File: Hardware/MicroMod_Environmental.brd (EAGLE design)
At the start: 46.5 x 38 mm, 26 parts, among them J1 MICROMOD_STANDARD, U1 SGP40, U3 SHTC3, U4 3.3V, U5 STC31

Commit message: Routed
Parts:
- added U2: EEPROM, SparkFun-IC-Memory:SO08
- C3, C4: device SparkFun-Capacitors:0603@1 -> SparkFun-Capacitors:0603
- C5, C6: device SparkFun-Capacitors:0402-TIGHT -> SparkFun-Capacitors:0603
- R12: value 100K -> 100k; device SparkFun-Resistors:0402 -> SparkFun-Resistors:0603
- R3: device SparkFun-Resistors:0402-TIGHT -> SparkFun-Resistors:0603
- moved R1 90.1 mm to (11.0, 13.1), turned to 270 degrees
- moved R2 88.3 mm to (9.02, 13.1), turned to 270 degrees
- moved R12 68.8 mm to (8.89, 29.2), turned to 90 degrees
- moved U4 61.4 mm to (13.0, 29.2), turned to 270 degrees
- moved C6 60.1 mm to (12.7, 32.0)
- moved C5 53.5 mm to (16.6, 31.2), turned to 90 degrees
- moved R3 47.1 mm to (62.2, 2.67)
- moved PWR\ 46.6 mm to (62.2, 6.93), turned to 180 degrees
- moved LED2 45.8 mm to (62.1, 4.57)
- moved C4 38.5 mm to (29.3, 19.3), turned to 90 degrees
- moved JP1 38.4 mm to (9.91, 10.2)
- moved 0X2A 36.7 mm to (28.3, 29.0)
- moved R6 36.2 mm to (25.0, 33.9)
- moved R5 32.2 mm to (25.0, 31.5)
- moved U5 32.1 mm to (33.8, 19.1), turned to 270 degrees
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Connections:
- removed net GND1: LED2.C
- new net A0: J1.36, U2.1
- new net A1: J1.34, U2.2
- new net A2: J1.32, U2.3
- net 3.3V: now also U2.8; no longer J1.73
- net GND: now also LED2.C, U2.4, U2.7
- net SCL: now also U2.6
- net SDA: now also U2.5
- net VCC: now also J1.72, J1.74
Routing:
- net 3.3V: track 0.00 -> 132.5 mm, vias 0 -> 5
- net SCL: track 0.00 -> 102.3 mm, vias 0 -> 2
- net SDA: track 0.00 -> 96.0 mm, vias 0 -> 2
- net ADDR: track 0.00 -> 19.4 mm, vias 0 -> 2
- net VCC: track 0.00 -> 11.3 mm, vias 0 -> 1
- net EN: track 0.00 -> 10.9 mm
- net A0: track 0.00 -> 8.10 mm, vias 0 -> 1
- net A1: track 0.00 -> 7.78 mm, vias 0 -> 1
- net A2: track 0.00 -> 7.46 mm, vias 0 -> 1
- net N$2: track 0.00 -> 6.95 mm, vias 0 -> 2
- net N$1: track 0.00 -> 4.88 mm
- net GND: track 0.00 -> 3.43 mm, vias 0 -> 16
- net N$3: track 0.00 -> 2.26 mm
- net N$4: track 0.00 -> 2.13 mm
- net N$7: track 0.00 -> 2.07 mm
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- added copper zone on layer 1, net 3.3V
- added copper zone on layer 1, net GND
- added copper zone on layer 16, net GND
- added copper zone on layer 16, net VCC
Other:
- board size 46.5 x 38 mm -> 65 x 38 mm

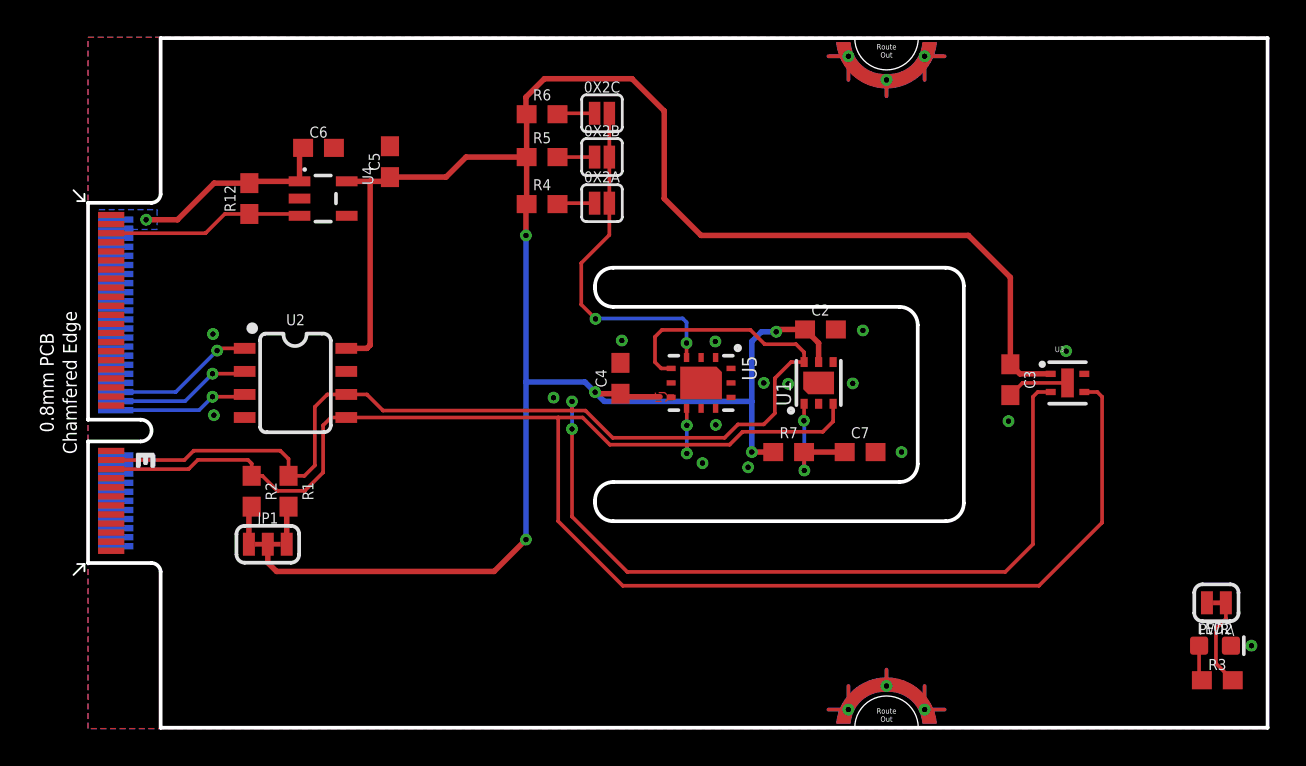
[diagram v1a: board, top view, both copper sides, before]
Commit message: Small tweaks to traces
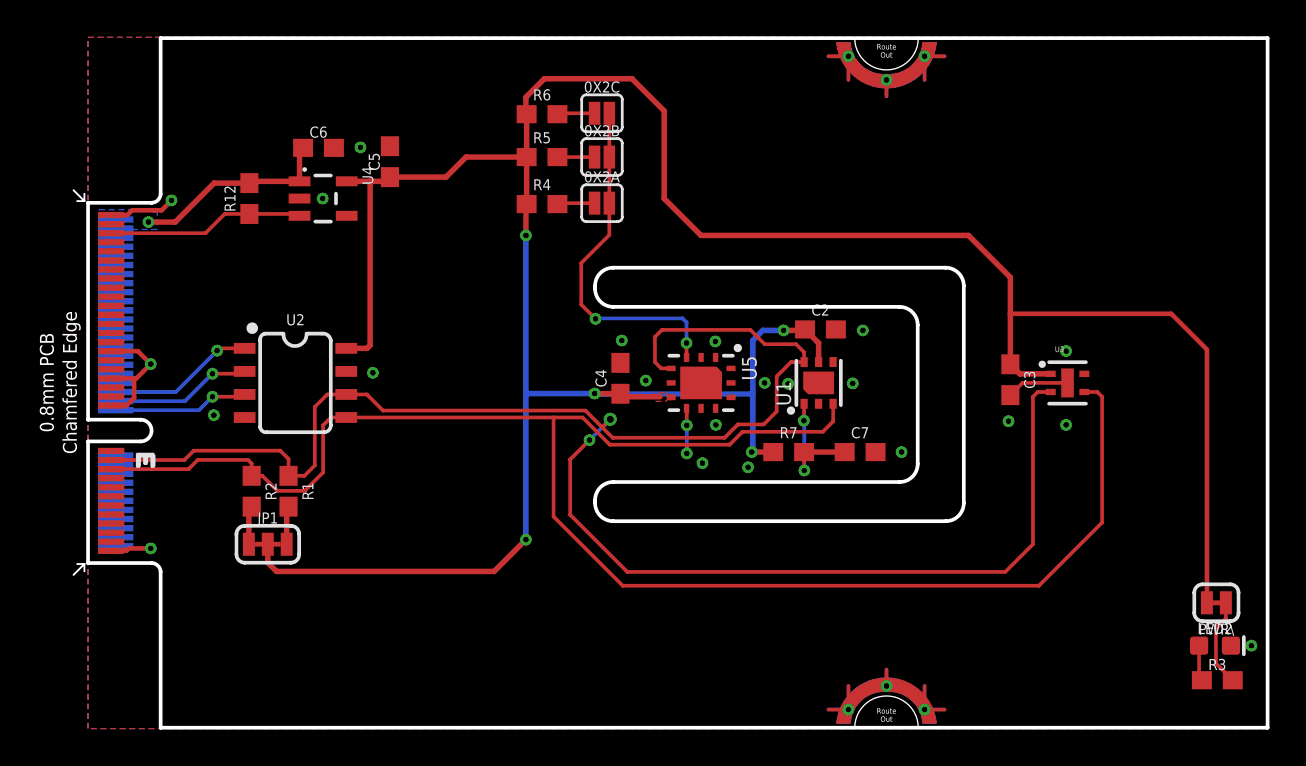
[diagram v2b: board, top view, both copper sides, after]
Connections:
- removed net 3.3V1: PWR\.2
- net 3.3V: now also PWR\.2
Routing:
- net 3.3V: track 132.5 -> 157.7 mm
- net GND: track 3.43 -> 27.4 mm, vias 16 -> 22

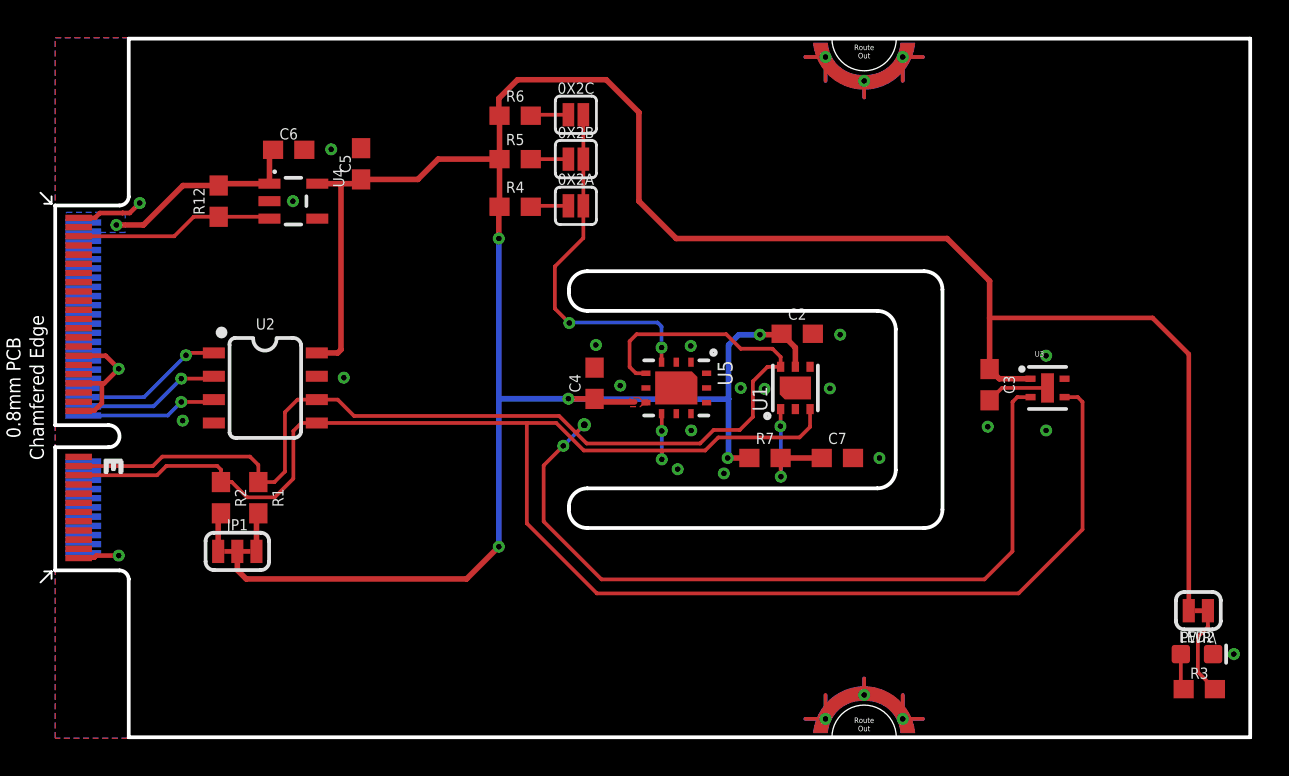
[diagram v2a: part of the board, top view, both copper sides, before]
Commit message: Adds silk, fiducials, and version number
* Adds text to part boxes in schematic
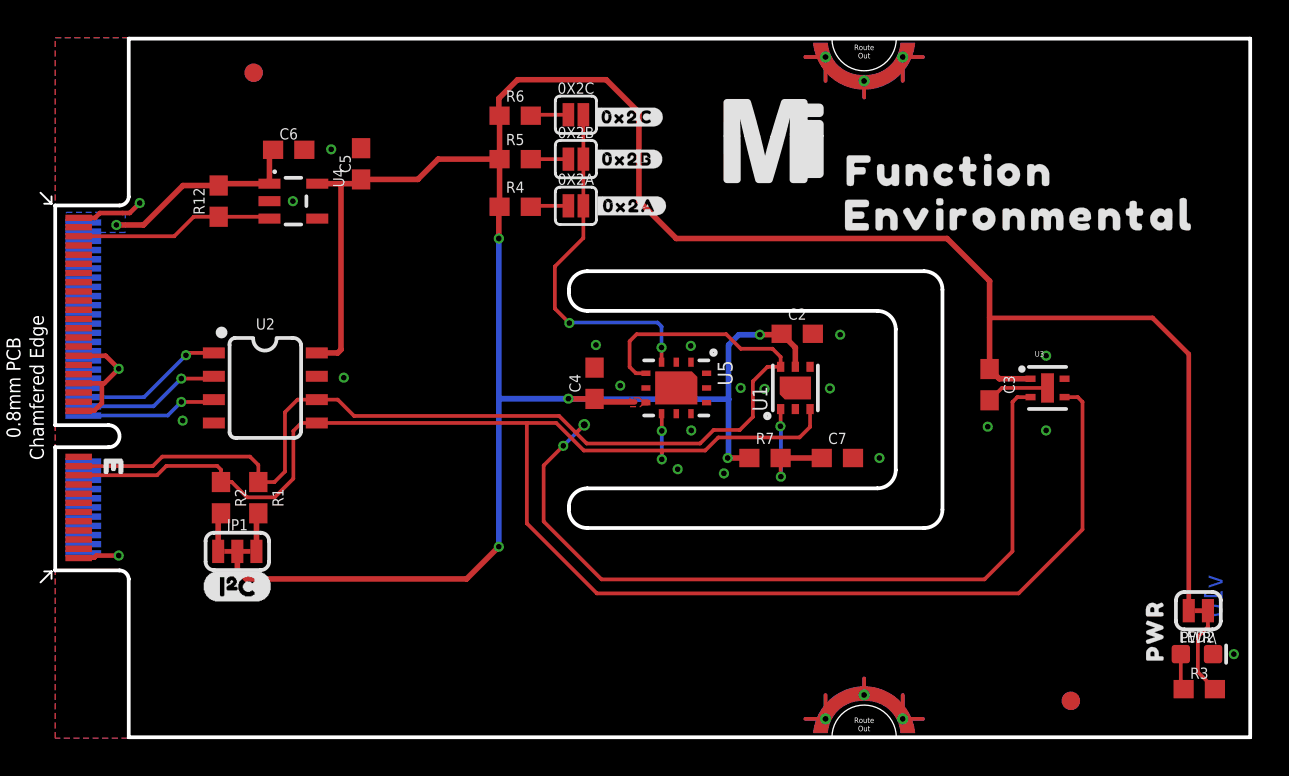
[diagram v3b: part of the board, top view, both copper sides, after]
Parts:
- added FD1, FD2, FD3, FD4: FIDUCIAL1X2, SparkFun-Aesthetics:FIDUCIAL-1X2
- added LOGO1: SFE_LOGO_NAME_FLAME.2_INCH, SparkFun-Aesthetics:SFE_LOGO_NAME_FLAME_.2
- added LOGO2: OSHW-LOGOS, SparkFun-Aesthetics:OSHW-LOGO-S
- added U$1: (no value), top:#0X2A#21
- added U$2: (no value), top:#0X2B#21
- added U$3: (no value), top:#0X2C#21
- added U$4: (no value), top:PWR321541
- added U$5: (no value), top:FUNCTION524
- added U$6: (no value), top:ENVIRONMENTAL526
- added U$7: (no value), SparkFun-MicroMod:MICROMOD_MI_LOGO_1
- added U$8: (no value), SparkFun-Buzzard:I2C
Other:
- board text added: "v10"
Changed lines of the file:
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@@
 <setting verticaltext="up"/>
 </settings>
-<grid distance="0.01" unitdist="inch" unit="inch" style="dots" multiple="1" display="yes" altdistance="0.001" altunitdist="inch" altunit="inch"/>
+<grid distance="0.05" unitdist="inch" unit="inch" style="dots" multiple="1" display="yes" altdistance="0.005" altunitdist="inch" altunit="inch"/>
 <layers>
 <layer number="1" name="Top" color="4" fill="1" visible="yes" active="yes"/>
@@
 <wire x1="28.94" y1="11.43" x2="47.26" y2="11.43" width="0.2032" layer="20"/>
 <wire x1="28.94" y1="13.589" x2="27.94" y2="12.589" width="0.2032" layer="20" curve="90"/>
+<text x="63.5" y="8.89" size="1.016" layer="16" font="vector" ratio="20" rot="SMR270">v10</text>
 </plain>
 <attributes>
@@
 </class>
 </classes>
-<designrules name="SparkFun-2-Layer-General-JLCPCB">
-<description language="en">&lt;b&gt;2 Layer General Rules for JLCPCB&lt;/b&gt;
+<designrules name="SparkFun-2-Layer-Minimum-JLCPCB">
+<description language="en">&lt;b&gt;2 Layer Minimum Rules for JLCPCB&lt;/b&gt;
 &lt;p&gt;
-These are the free and generally easy to produce 2-layer PCB design rules. You can certainly go smaller but if the design doesn't call for it, these rules provide good guidance.
+These are the minimums &lt;a href=&quot;https://jlcpcb.com/capabilities/Capabilities&quot;&gt;quoted by JLCPCB&lt;/a&gt; to produce a 2-layer PCB design rules. These rules are &quot;free&quot; and generally low-cost. Going below these settings may cause the board to be not manufacturable or incur a price increase.
 &lt;ul&gt;
 &lt;li&gt;2 Layer&lt;/li&gt;
-&lt;li&gt;7mil Trace/Space&lt;/li&gt;
-&lt;li&gt;7mil Annular Rings&lt;/li&gt;
+&lt;li&gt;5mil Trace/Space&lt;/li&gt;
+&lt;li&gt;5mil Annular Rings&lt;/li&gt;
 &lt;li&gt;12mil Vias&lt;/li&gt;
-&lt;li&gt;3mil Stop Mask&lt;/li&gt;
+&lt;li&gt;2.5mil Stop Mask&lt;/li&gt;
 &lt;/ul&gt;</description>
 <param name="layerSetup" value="(1*16)"/>
 <param name="mtCopper" value="0.035mm 0.035mm 0.035mm 0.035mm 0.035mm 0.035mm 0.035mm 0.035mm 0.035mm 0.035mm 0.035mm 0.035mm 0.035mm 0.035mm 0.035mm 0.035mm"/>
 <param name="mtIsolate" value="1.5mm 0.15mm 0.2mm 0.15mm 0.2mm 0.15mm 0.2mm 0.15mm 0.2mm 0.15mm 0.2mm 0.15mm 0.2mm 0.15mm 0.2mm"/>
-<param name="mdWireWire" value="7mil"/>
-<param name="mdWirePad" value="7mil"/>
-<param name="mdWireVia" value="7mil"/>
-<param name="mdPadPad" value="7mil"/>
-<param name="mdPadVia" value="7mil"/>
-<param name="mdViaVia" value="7mil"/>
-<param name="mdSmdPad" value="7mil"/>
-<param name="mdSmdVia" value="7mil"/>
-<param name="mdSmdSmd" value="7mil"/>
+<param name="mdWireWire" value="5mil"/>
+<param name="mdWirePad" value="5mil"/>
+<param name="mdWireVia" value="5mil"/>
+<param name="mdPadPad" value="5mil"/>
+<param name="mdPadVia" value="5mil"/>
+<param name="mdViaVia" value="5mil"/>
+<param name="mdSmdPad" value="5mil"/>
+<param name="mdSmdVia" value="5mil"/>
+<param name="mdSmdSmd" value="5mil"/>
 <param name="mdViaViaSameLayer" value="8mil"/>
 <param name="mnLayersViaInSmd" value="2"/>
@@
 <param name="mdDrill" value="7mil"/>
 <param name="mdSmdStop" value="0mil"/>
-<param name="msWidth" value="7mil"/>
+<param name="msWidth" value="5mil"/>
 <param name="msDrill" value="0.3mm"/>
 <param name="msMicroVia" value="9.99mm"/>
@@
 <param name="rvMicroViaOuter" value="0.25"/>
 <param name="rvMicroViaInner" value="0.25"/>
-<param name="rlMinPadTop" value="7mil"/>
+<param name="rlMinPadTop" value="5mil"/>
 <param name="rlMaxPadTop" value="20mil"/>
-<param name="rlMinPadInner" value="7mil"/>
+<param name="rlMinPadInner" value="5mil"/>
 <param name="rlMaxPadInner" value="20mil"/>
-<param name="rlMinPadBottom" value="7mil"/>
+<param name="rlMinPadBottom" value="5mil"/>
 <param name="rlMaxPadBottom" value="20mil"/>
-<param name="rlMinViaOuter" value="7mil"/>
+<param name="rlMinViaOuter" value="5mil"/>
 <param name="rlMaxViaOuter" value="20mil"/>
-<param name="rlMinViaInner" value="7mil"/>
+<param name="rlMinViaInner" value="5mil"/>
 <param name="rlMaxViaInner" value="20mil"/>
 <param name="rlMinMicroViaOuter" value="4mil"/>
@@
 <param name="mvStopFrame" value="1"/>
 <param name="mvCreamFrame" value="0"/>
-<param name="mlMinStopFrame" value="3mil"/>
-<param name="mlMaxStopFrame" value="3mil"/>
+<param name="mlMinStopFrame" value="2.5mil"/>
+<param name="mlMaxStopFrame" value="2.5mil"/>
 <param name="mlMinCreamFrame" value="0mil"/>
 <param name="mlMaxCreamFrame" value="0mil"/>
@@
 <attribute name="VALUE" x="11.43" y="15.24" size="0.6096" layer="27" font="vector" ratio="20" align="bottom-center"/>
 </element>
+<element name="LOGO1" library="SparkFun-Aesthetics" package="SFE_LOGO_NAME_FLAME_.2" value="SFE_LOGO_NAME_FLAME.2_INCH" x="24.511" y="4.572" smashed="yes" rot="MR0"/>
+<element name="LOGO2" library="SparkFun-Aesthetics" package="OSHW-LOGO-S" value="OSHW-LOGOS" x="7.62" y="35.052" smashed="yes" rot="MR0"/>
+<element name="FD1" library="SparkFun-Aesthetics" package="FIDUCIAL-1X2" value="FIDUCIAL1X2" x="10.795" y="36.195" smashed="yes"/>
+<element name="FD2" library="SparkFun-Aesthetics" package="FIDUCIAL-1X2" value="FIDUCIAL1X2" x="10.795" y="36.195" smashed="yes" rot="MR0"/>
+<element name="FD3" library="SparkFun-Aesthetics" package="FIDUCIAL-1X2" value="FIDUCIAL1X2" x="55.245" y="2.032" smashed="yes" rot="MR0"/>
+<element name="FD4" library="SparkFun-Aesthetics" package="FIDUCIAL-1X2" value="FIDUCIAL1X2" x="55.245" y="2.032" smashed="yes"/>
+<element name="U$1" library="top" package="#0X2A#21" value="" x="31.242" y="28.956" smashed="yes"/>
+<element name="U$2" library="top" package="#0X2B#21" value="" x="31.115" y="31.496" smashed="yes"/>
+<element name="U$3" library="top" package="#0X2C#21" value="" x="31.115" y="33.782" smashed="yes"/>
+<element name="U$4" library="top" package="PWR321541" value="" x="59.817" y="5.842" smashed="yes" rot="R90"/>
+<element name="U$5" library="top" package="FUNCTION524" value="" x="48.641" y="30.861" smashed="yes"/>
+<element name="U$6" library="top" package="ENVIRONMENTAL526" value="" x="52.451" y="28.448" smashed="yes"/>
+<element name="U$7" library="SparkFun-MicroMod" package="MICROMOD_MI_LOGO_1" value="" x="39.116" y="32.512" smashed="yes"/>
+<element name="U$8" library="SparkFun-Buzzard" package="I2C" value="" x="8.001" y="8.255" smashed="yes"/>
 </elements>
 <signals>
@@
 <wire x1="1.275" y1="28.3" x2="2.164" y2="28.3" width="0.254" layer="1"/>
 <wire x1="2.428" y1="28.564" x2="3.6637375" y2="28.564" width="0.254" layer="1"/>
-<wire x1="3.6637375" y1="28.564" x2="3.6747375" y2="28.575" width="0.254" layer="1"/>
 <via x="3.4544" y="9.9314" extent="1-16" drill="0.3048"/>
 <wire x1="1.275" y1="9.8" x2="1.2952" y2="9.8202" width="0.254" layer="1"/>
@@
 <contactref element="R1" pad="2"/>
 <contactref element="JP1" pad="3"/>
-<wire x1="10.9474" y1="10.16" x2="11.049" y2="10.2616" width="0.2032" layer="1"/>
 <wire x1="10.9474" y1="10.16" x2="10.9474" y2="12.1294" width="0.3048" layer="1"/>
 <wire x1="10.9474" y1="12.1294" x2="11.049" y2="12.231" width="0.3048" layer="1"/>
@@
 <mfgpreviewcolor name="substratecolor" color="0xFF786E46"/>
 </mfgpreviewcolors>
+<errors>
+</errors>
 </board>
 </drawing>

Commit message: Reroutes board
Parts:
- removed LED2: RED, SparkFun-LED:LED-0603
- added LED1: RED, SparkFun-LED:LED-0603
- moved PWR\ 29.3 mm to (62.0, 36.2), turned to 90 degrees
- moved U$4 28.4 mm to (62.2, 34.2), turned to 0 degrees
- moved R3 27.9 mm to (62.2, 30.6)
- moved C3 25.4 mm to (25.5, 21.7), turned to 0 degrees
- moved C7 21.1 mm to (21.5, 15.0), turned to 180 degrees
- moved U3 21.1 mm to (32.9, 19.1), turned to 180 degrees
- moved U1 15.9 mm to (24.4, 19.1)
- moved R7 13.1 mm to (25.5, 15.0), turned to 180 degrees
- moved U5 8.89 mm to (42.7, 19.1)
- moved C4 6.26 mm to (35.6, 18.9)
- moved C2 3.28 mm to (39.3, 18.9), turned to 90 degrees
- moved R12 0.76 mm to (9.65, 29.2)
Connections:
- net GND: now also LED1.C; no longer LED2.C
- net N$10: now also LED1.A; no longer LED2.A
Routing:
- net SCL: track 102.4 -> 50.8 mm, vias 2 -> 0
- net SDA: track 96.1 -> 50.8 mm, vias 2 -> 0
- net 3.3V: track 157.7 -> 120.1 mm, vias 5 -> 6
- net ADDR: track 19.4 -> 26.3 mm, vias 2 -> 0
- net N$2: track 6.95 -> 5.34 mm
- net GND: track 27.4 -> 26.1 mm, vias 22 -> 21
- net N$1: track 4.88 -> 5.54 mm
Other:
- outline, holes or cut-outs redrawn
